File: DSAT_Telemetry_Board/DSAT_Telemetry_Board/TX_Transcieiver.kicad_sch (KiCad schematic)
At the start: 4 parts

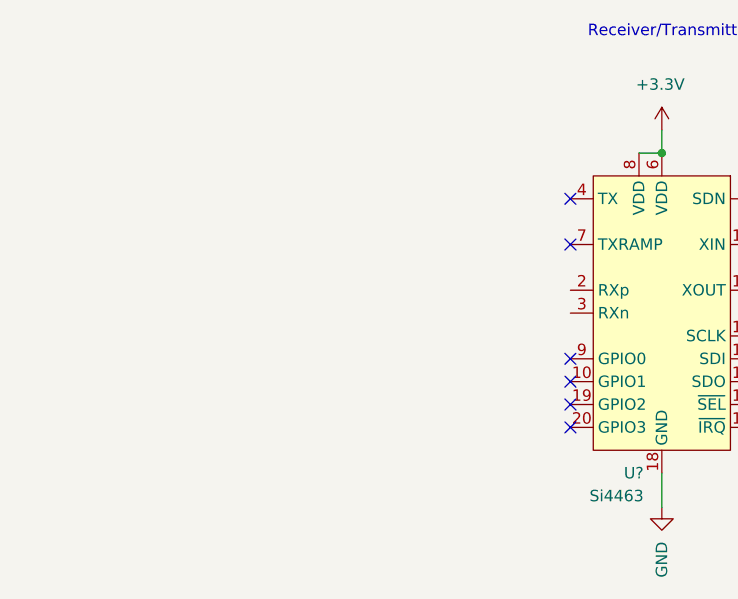
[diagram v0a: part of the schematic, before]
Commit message: antenna matching netowrks for Rx and Tx added partially
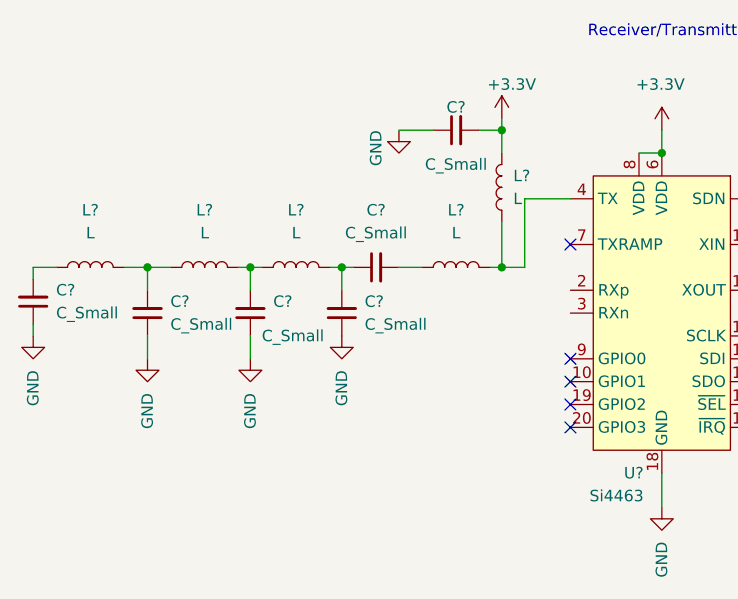
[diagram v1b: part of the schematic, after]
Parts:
- added C? (x6): C_Small, symbol Device:C_Small
- added L? (x5): L, symbol Device:L
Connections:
- net +3.3V: now also C?.2, L?.2
- net GND: now also C?.1, C?.1, C?.1, C?.1, C?.1
- net at U?.4 (TX): now also L?.1, L?.2
- new net: C?.2, L?.1 (x2)
- new net: C?.2, L?.1, L?.2 (x2)
- new net: C?.1, C?.2, L?.2
- no-connect marks 6 -> 5

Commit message: Testing
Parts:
- C? (x2): value Unknown -> 20uF
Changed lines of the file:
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@@
       (effects (font (size 1.27 1.27)) (justify right))
     )
-    (property "Value" "Unknown" (id 1) (at 156.21 104.14 0)
+    (property "Value" "20uF" (id 1) (at 156.21 104.14 0)
       (effects (font (size 1.27 1.27)) (justify right))
     )
@@
       (effects (font (size 1.27 1.27)) (justify left))
     )
-    (property "Value" "Unknown" (id 1) (at 189.23 102.8699 0)
+    (property "Value" "20uF" (id 1) (at 189.23 102.8699 0)
       (effects (font (size 1.27 1.27)) (justify left))
     )

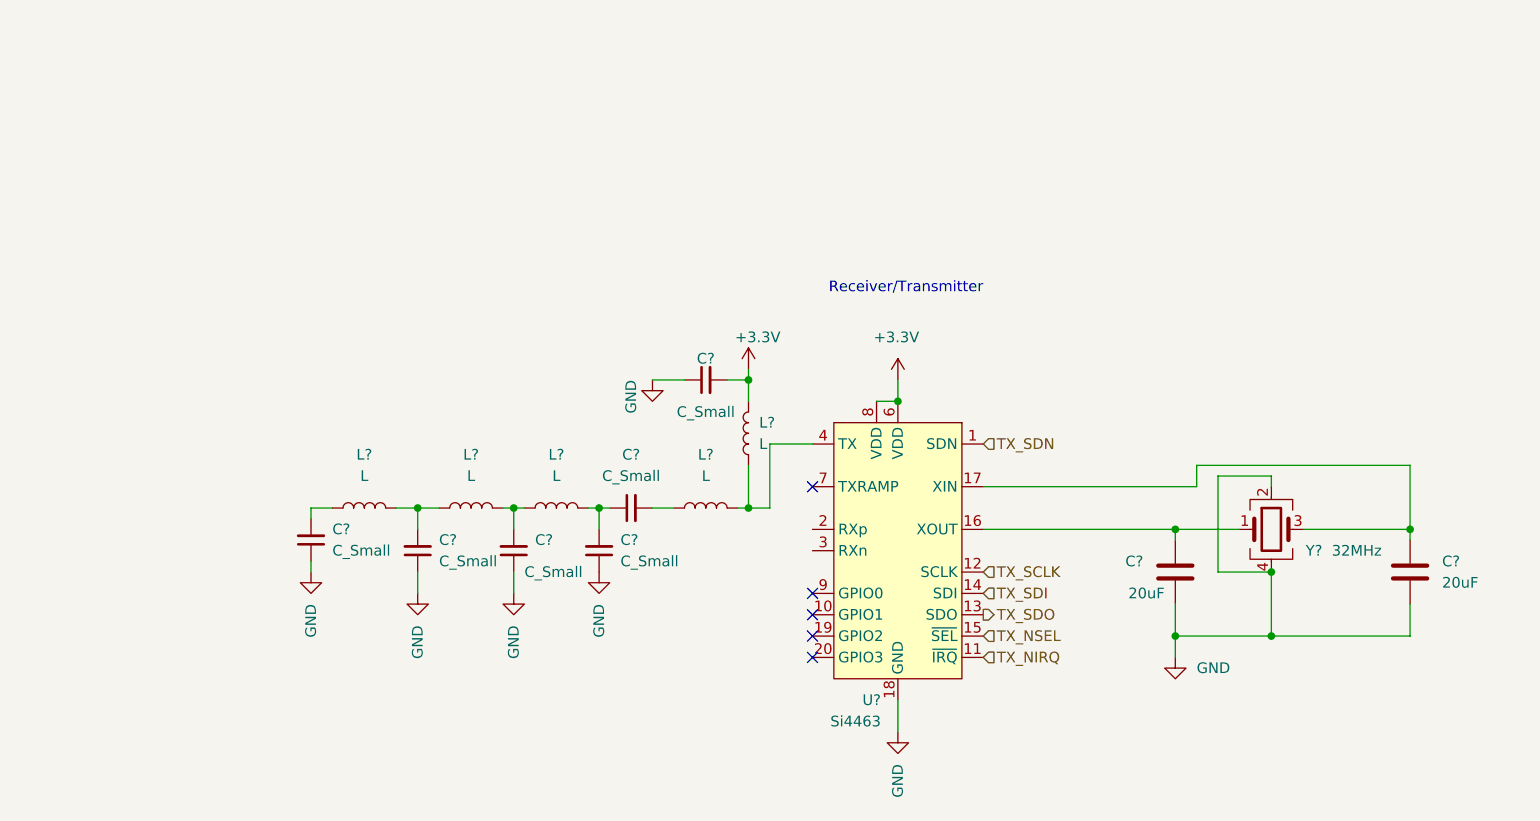
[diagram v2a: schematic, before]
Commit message: Added Transciever Updates/Biases/RF_Switch
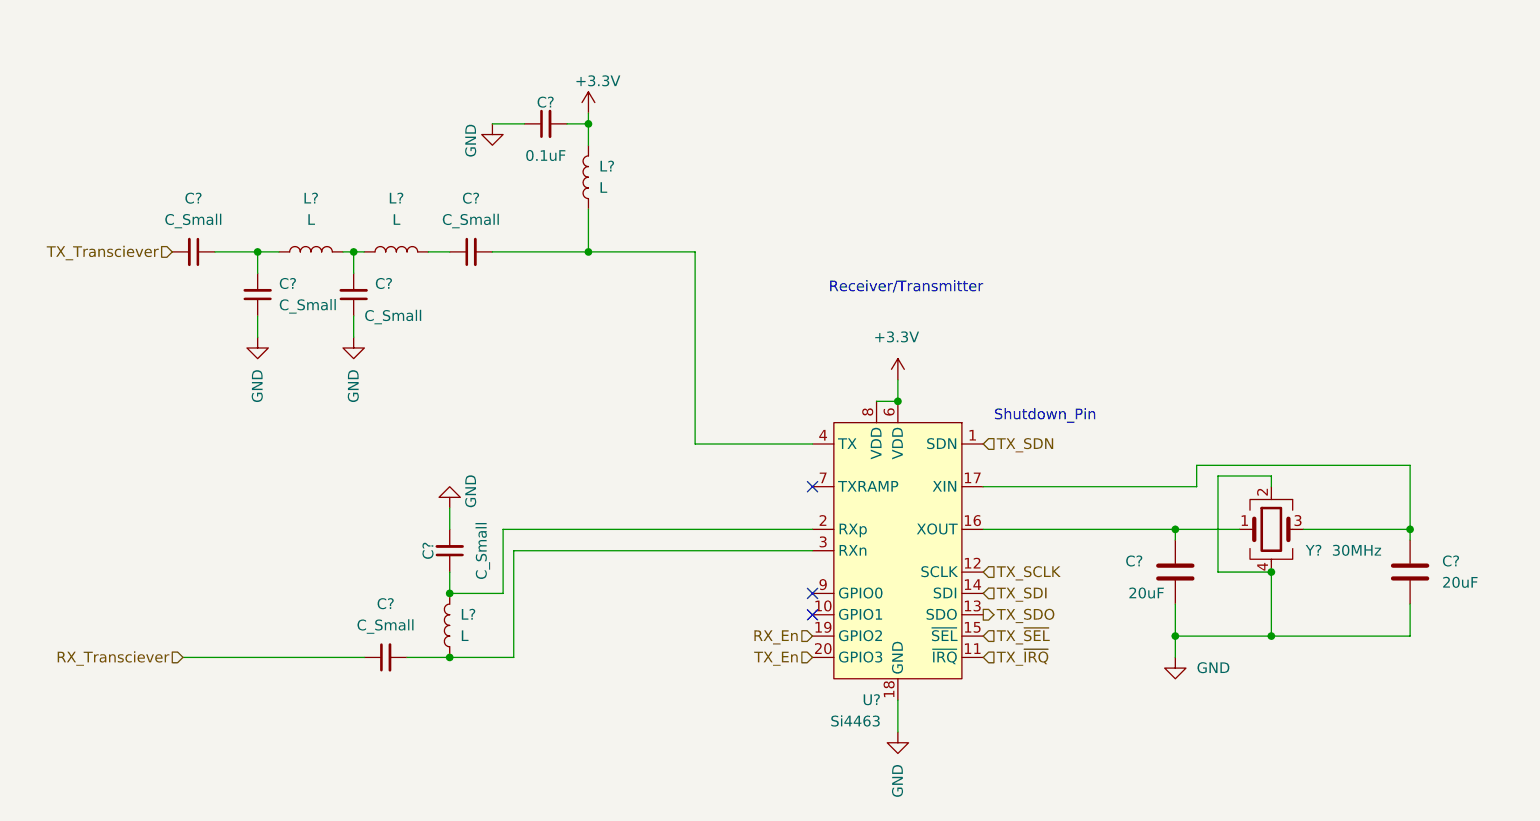
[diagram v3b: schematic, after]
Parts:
- removed C? (x2): C_Small, symbol Device:C_Small
- removed L? (x2): L, symbol Device:L
- added C? (x3): C_Small, symbol Device:C_Small
- added L?: L, symbol Device:L
- C?: value C_Small -> 0.1uF
- Y?: value 32MHz -> 30MHz
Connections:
- net GND: now also C?.2
- net RX_En: now reaches U?.19 (GPIO2)
- net at U?.2 (RXp): now also C?.1, L?.2
- net TX_En: now reaches U?.20 (GPIO3)
- net at U?.3 (RXn): now also C?.2, L?.1
- net at L?.1, U?.4 (TX): now also C?.2
- net at C?.2, L?.1: now also C?.1
- net TX_NIRQ renamed TX_~{IRQ}
- net TX_NSEL renamed TX_~{SEL}
- new net RX_Transciever: C?.1
- new net TX_Transciever: C?.2
- no-connect marks 5 -> 3
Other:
- note added: "Shutdown_Pin"
- moved on the sheet: C?, L?

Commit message: Added Matching Networks/Linear Regulator/Watchdog Pins
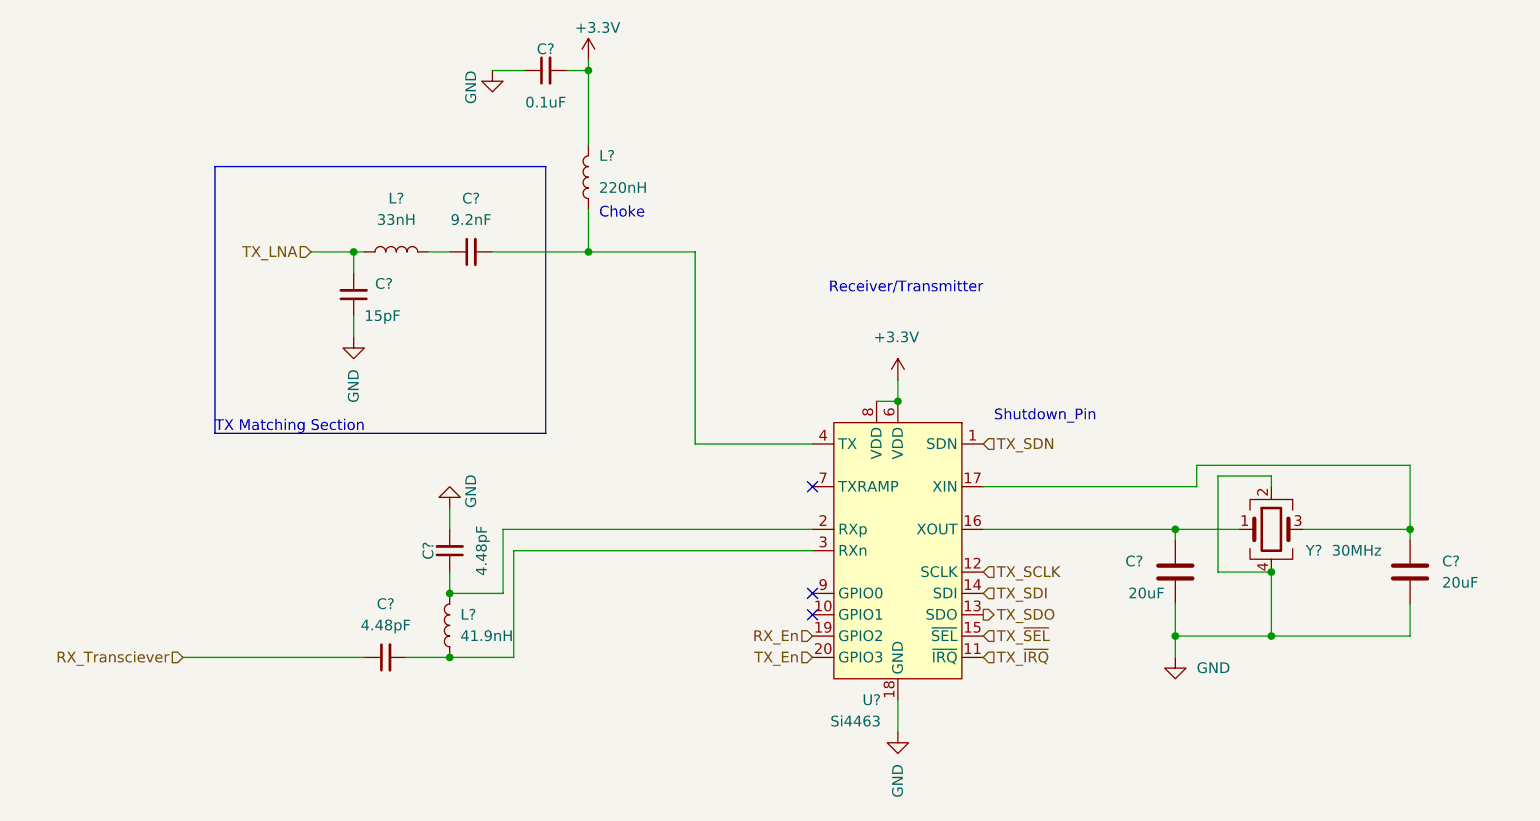
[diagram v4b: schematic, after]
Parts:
- removed C? (x2): C_Small, symbol Device:C_Small
- removed L?: L, symbol Device:L
- C?: value C_Small -> 9.2nF
- C?: value C_Small -> 15pF
- C? (x2): value C_Small -> 4.48pF
- L?: value L -> 33nH
- L?: value L -> 41.9nH
- L?: value L -> 220nH
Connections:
- net TX_LNA: now reaches C?.2, L?.1
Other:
- note added: "Choke"
- note added: "TX Matching Section"
- moved on the sheet: C?

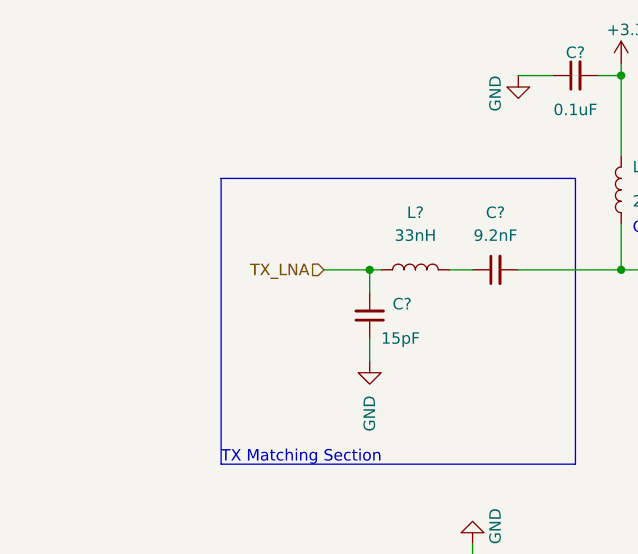
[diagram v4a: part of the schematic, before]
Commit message: Transceiver sheet - replaced TX_LNA with TX_Transceiver
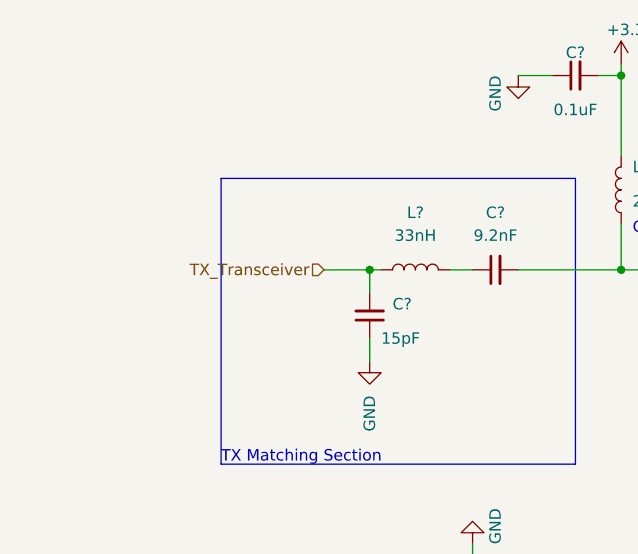
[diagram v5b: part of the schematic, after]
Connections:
- net TX_LNA renamed TX_Transceiver
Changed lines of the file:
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@@
     (effects (font (size 1.27 1.27)) (justify right))
   )
-  (hierarchical_label "TX_LNA" (shape input) (at 54.61 63.5 180)
+  (hierarchical_label "TX_Transceiver" (shape input) (at 54.61 63.5 180)
     (effects (font (size 1.27 1.27)) (justify right))
   )
